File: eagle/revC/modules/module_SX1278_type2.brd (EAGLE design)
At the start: 24.1 x 32.8 mm, 19 parts, among them X1 734120110

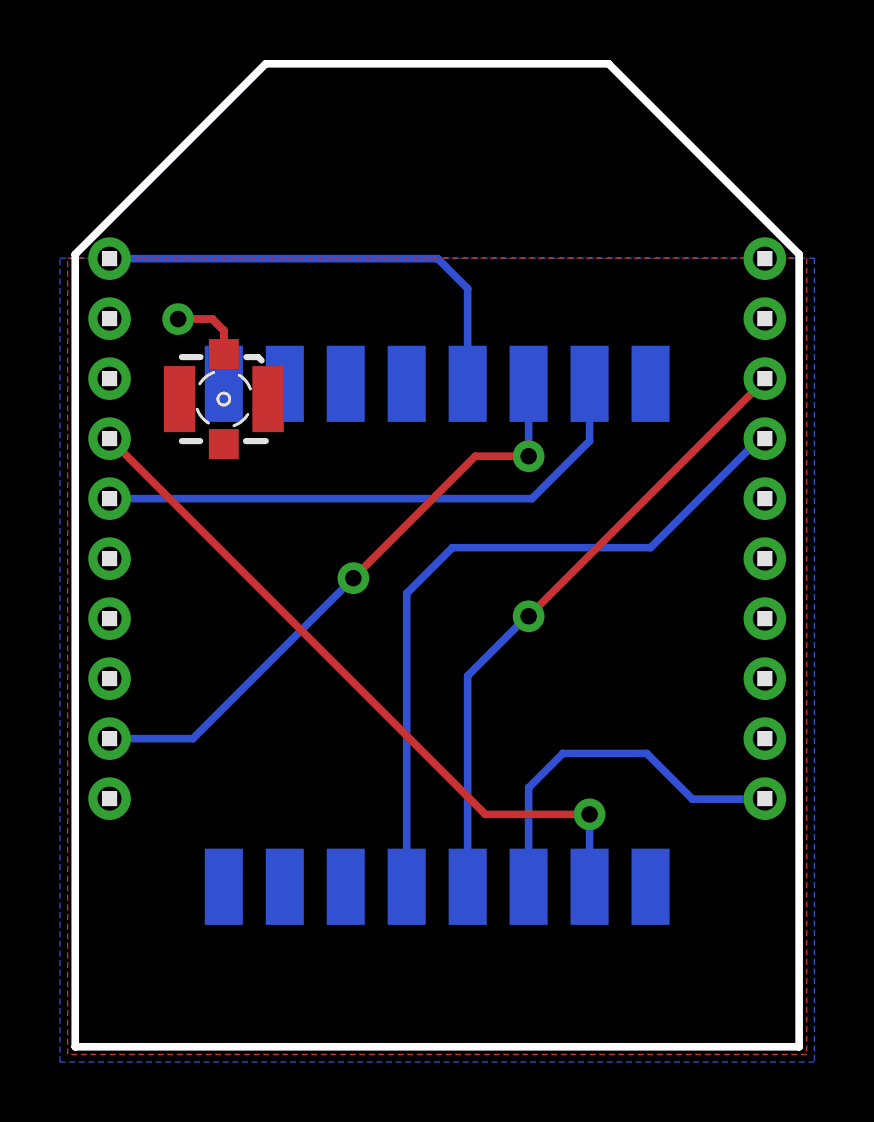
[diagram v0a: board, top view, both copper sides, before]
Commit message: Replaced modules with library parts
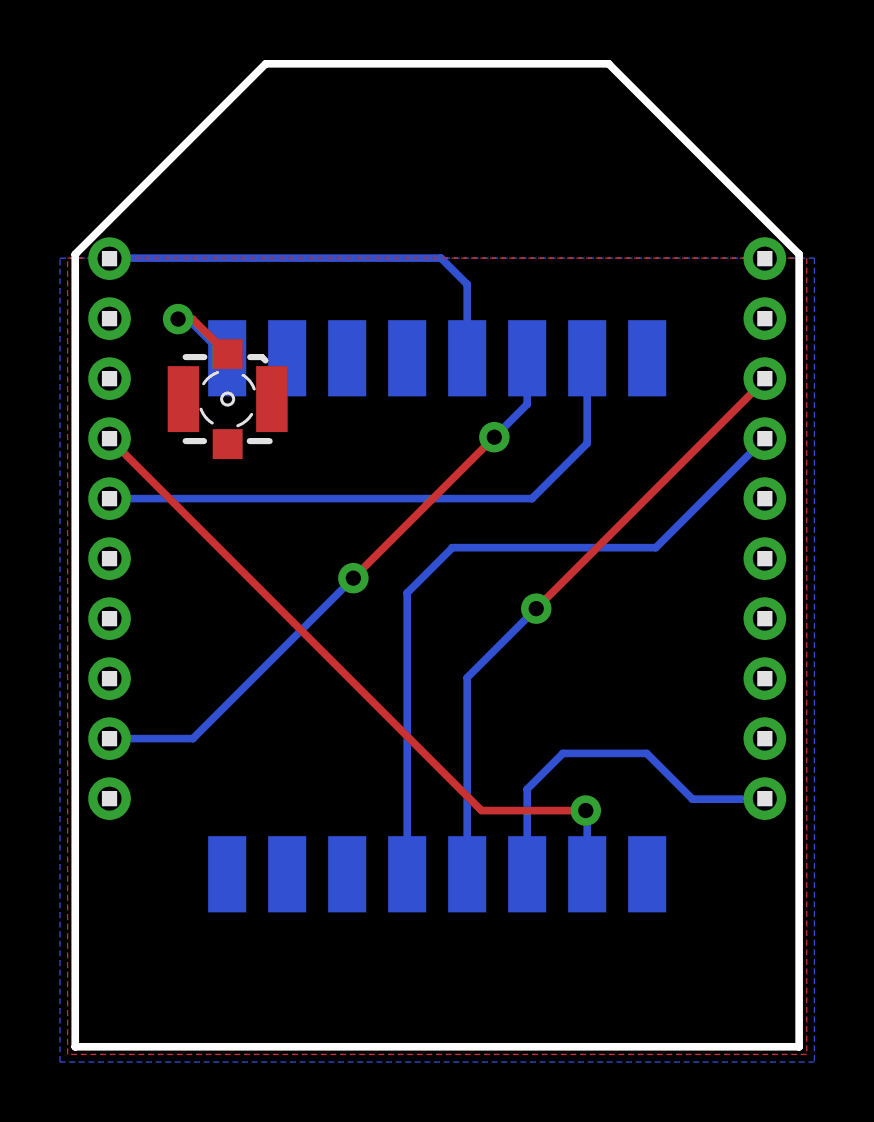
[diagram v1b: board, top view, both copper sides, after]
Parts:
- removed DIO0, DIO1, DIO2, DIO3, DIO4, DIO5, GND, GND2, GND_ANT, NSS, RF, RST, SCK, SI, SO, VCC: (no value), wirepad:SMD1,27-2,54
- added U$1: SX1278_2, RadioShield:SX1278_2
- moved X1 0.13 mm to (5.21, 21.7)
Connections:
- removed net ANT: RF.1, X1.1
- removed net INT0: DIO0.1, LEFT1.9
- removed net INT1: DIO1.1, LEFT1.5
- removed net SCPI_SCK: RIGHT1.3, SCK.1
- removed net SPI_CS: NSS.1, RIGHT1.4
- removed net SPI_MISO: LEFT1.4, SO.1
- removed net SPI_MOSI: RIGHT1.10, SI.1
- removed net VCC: LEFT1.1, VCC.1
- new net N$1: U$1.ANT, X1.1
- new net N$2: LEFT1.9, U$1.DIO0
- new net N$3: RIGHT1.10, U$1.MOSI
- new net N$4: RIGHT1.4, U$1.NSS
- new net N$5: RIGHT1.3, U$1.SCK
- new net N$6: LEFT1.5, U$1.DIO1
- new net N$7: LEFT1.4, U$1.MISO
- new net N$8: LEFT1.1, U$1.VCC
- net GND: now also U$1.GND@1, U$1.GND@2, U$1.GND@3; no longer GND.1, GND2.1, GND_ANT.1
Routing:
- net SPI_CS: track 23.9 -> 0.00 mm
- net SPI_MISO: track 23.6 -> 0.00 mm, vias 1 -> 0
- net N$4: track 0.00 -> 23.4 mm
- net N$7: track 0.00 -> 23.2 mm, vias 0 -> 1
- net SCPI_SCK: track 21.1 -> 0.00 mm, vias 1 -> 0
- net N$5: track 0.00 -> 20.6 mm, vias 0 -> 1
- net INT0: track 20.3 -> 0.00 mm, vias 2 -> 0
- net N$2: track 0.00 -> 20.1 mm, vias 0 -> 2
- net N$6: track 0.00 -> 19.5 mm
- net INT1: track 18.7 -> 0.00 mm
- net VCC: track 15.5 -> 0.00 mm
- net N$8: track 0.00 -> 14.8 mm
- net SPI_MOSI: track 12.3 -> 0.00 mm
- net N$3: track 0.00 -> 11.9 mm
- net ANT: track 5.93 -> 0.00 mm, vias 1 -> 0
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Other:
- board text removed: "DIO0"
- board text removed: "DIO1"
- board text removed: "DIO2"
- board text removed: "DIO3"
- board text removed: "DIO4"
- board text removed: "DIO5"
- board text removed: "GND"
- board text removed: "NSS"
- board text removed: "RF"
- board text removed: "RST"
- board text removed: "SCK"
- board text removed: "SI"
- board text removed: "SO"
- board text removed: "VCC"

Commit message: Fixed module name layers
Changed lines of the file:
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@@
 <wire x1="24.257" y1="26.543" x2="24.257" y2="0.127" width="0.254" layer="20"/>
 <wire x1="24.257" y1="0.127" x2="0.127" y2="0.127" width="0.254" layer="20"/>
-<text x="12.192" y="30.48" size="1.778" layer="51" ratio="15" rot="SR0" align="center">SX1278</text>
+<text x="12.192" y="30.48" size="1.778" layer="25" ratio="15" rot="SR0" align="center">SX1278</text>
 </plain>
 <attributes>
